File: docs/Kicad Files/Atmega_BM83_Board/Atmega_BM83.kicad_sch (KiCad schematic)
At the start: 34 parts, among them J1 18V, J10 ICE Header, J2 Out to Amp, J3 PWR SW, J4 Volume POT, J5 Pairing BTN, J6 PWR LED, J7 Pair LED, J8 Conn_01x12, J9 Conn_01x12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

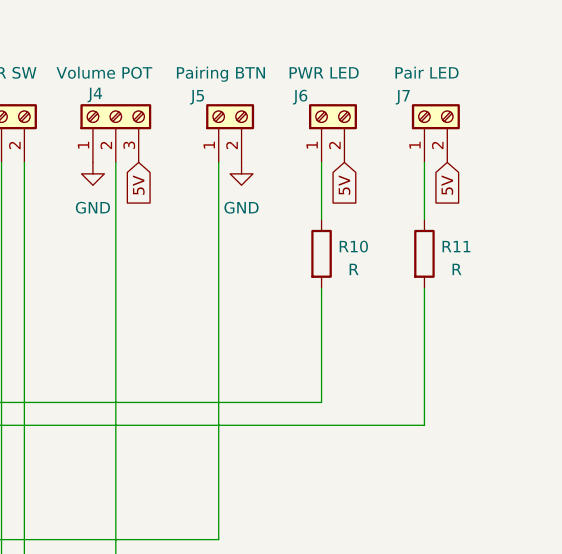
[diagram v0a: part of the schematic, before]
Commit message: all footprints assigned BM83/Atmega schematic
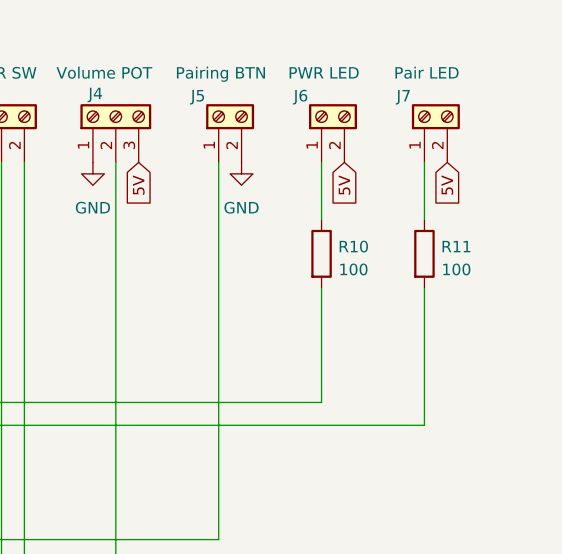
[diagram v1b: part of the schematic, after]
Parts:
- C1, C2, C3, C4: footprint (none) -> Capacitor_THT:CP_Radial_Tantal_D5.0mm_P5.00mm
- C6, C7: footprint (none) -> Capacitor_THT:C_Rect_L7.0mm_W2.5mm_P5.00mm
- J10: footprint Z_Custom_Footprints:ICE_Header -> Custom_Footprints:ICE_Header
- J4: footprint TerminalBlock_Phoenix:TerminalBlock_Phoenix_MKDS-1,5-3-5.08_1x03_P5.08mm_Horizontal -> TerminalBlock_Phoenix:TerminalBlock_Phoenix_MKDS-1,5-3_1x03_P5.00mm_Horizontal
- R10, R11: value R -> 100
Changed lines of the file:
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@@
 			)
 		)
-		(property "Footprint" ""
+		(property "Footprint" "Capacitor_THT:CP_Radial_Tantal_D5.0mm_P5.00mm"
 			(at 120.65 101.2952 0)
 			(effects
@@
 			)
 		)
-		(property "Footprint" ""
+		(property "Footprint" "Capacitor_THT:CP_Radial_Tantal_D5.0mm_P5.00mm"
 			(at 140.97 119.0752 0)
 			(effects
@@
 			)
 		)
-		(property "Footprint" ""
+		(property "Footprint" "Capacitor_THT:C_Rect_L7.0mm_W2.5mm_P5.00mm"
 			(at 163.5252 43.18 0)
 			(effects
@@
 			)
 		)
-		(property "Footprint" ""
+		(property "Footprint" "Capacitor_THT:CP_Radial_Tantal_D5.0mm_P5.00mm"
 			(at 69.85 101.9048 0)
 			(effects
@@
 			)
 		)
-		(property "Footprint" "Z_Custom_Footprints:ICE_Header"
+		(property "Footprint" "Custom_Footprints:ICE_Header"
 			(at 267.97 99.06 0)
 			(effects
@@
 			)
 		)
-		(property "Footprint" "TerminalBlock_Phoenix:TerminalBlock_Phoenix_MKDS-1,5-3-5.08_1x03_P5.08mm_Horizontal"
+		(property "Footprint" "TerminalBlock_Phoenix:TerminalBlock_Phoenix_MKDS-1,5-3_1x03_P5.00mm_Horizontal"
 			(at 238.76 25.4 0)
 			(effects
@@
 			)
 		)
-		(property "Value" "R"
+		(property "Value" "100"
 			(at 265.176 42.418 0)
 			(effects
@@
 			)
 		)
-		(property "Footprint" ""
+		(property "Footprint" "Capacitor_THT:C_Rect_L7.0mm_W2.5mm_P5.00mm"
 			(at 212.09 38.4048 0)
 			(effects
@@
 			)
 		)
-		(property "Footprint" ""
+		(property "Footprint" "Capacitor_THT:CP_Radial_Tantal_D5.0mm_P5.00mm"
 			(at 124.7648 45.72 0)
 			(effects
@@
 			)
 		)
-		(property "Value" "R"
+		(property "Value" "100"
 			(at 276.606 42.418 0)
 			(effects

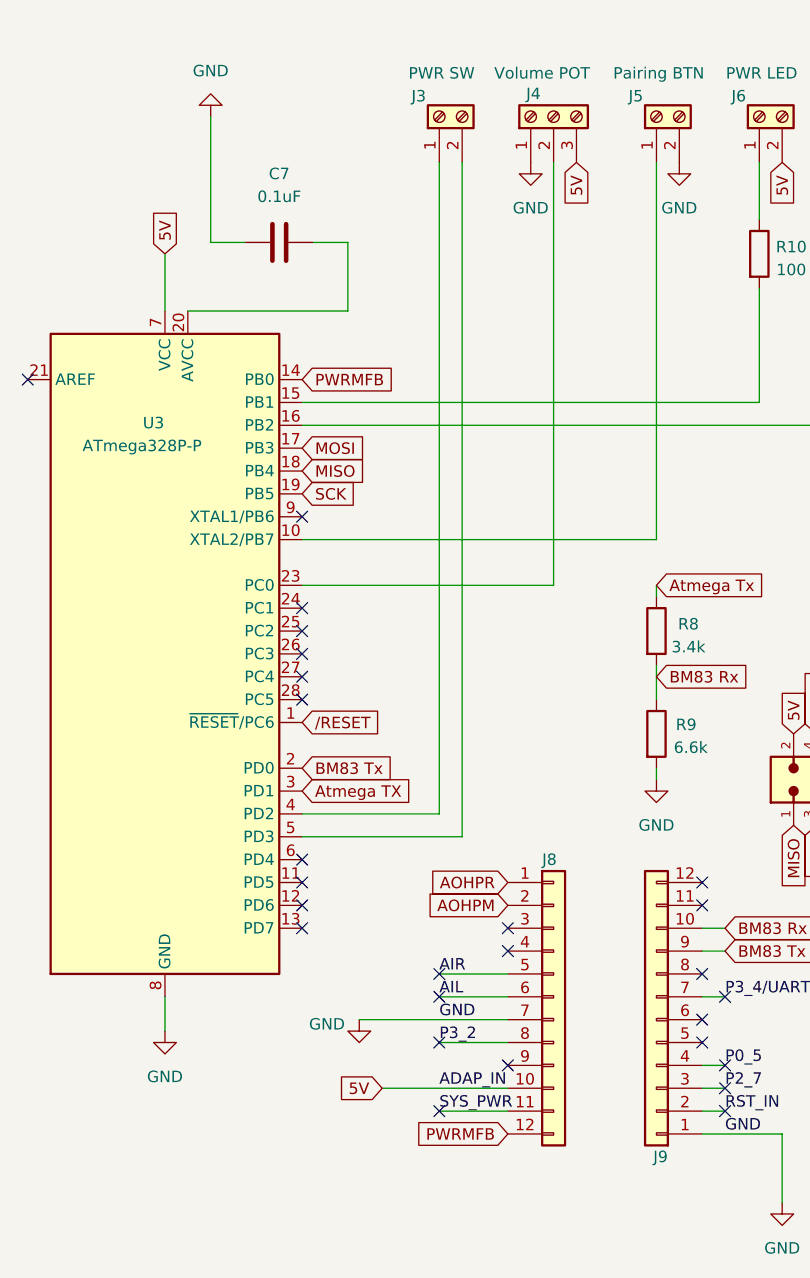
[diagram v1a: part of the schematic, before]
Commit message: changed volume switch and removed powerMFB
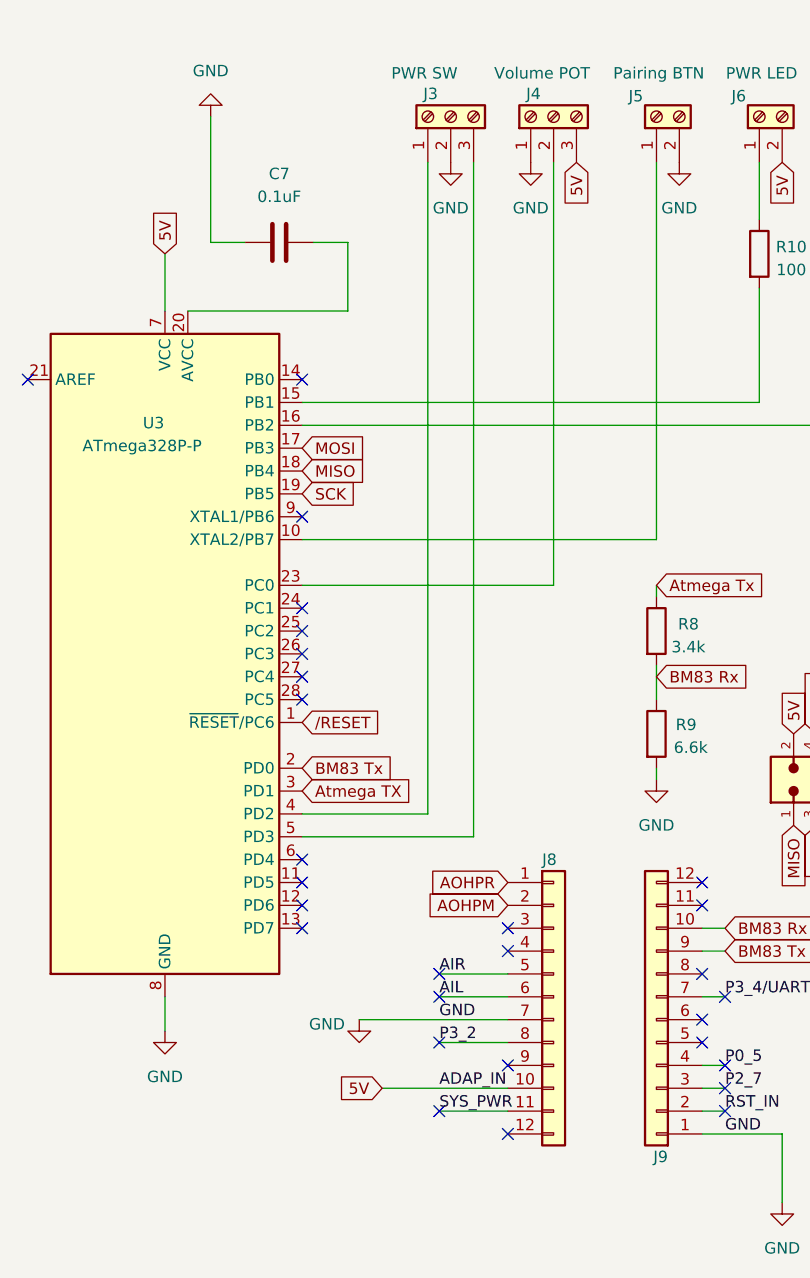
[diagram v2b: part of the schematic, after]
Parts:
- removed J3: PWR SW, TerminalBlock_Phoenix:TerminalBlock_Phoenix_MKDS-1,5-2_1x02_P5.00mm_Horizontal, symbol Connector:Screw_Terminal_01x02
- added J3: PWR SW, TerminalBlock_Phoenix:TerminalBlock_Phoenix_MKDS-1,5-3_1x03_P5.00mm_Horizontal, symbol Connector:Screw_Terminal_01x03
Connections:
- net GND: now also J3.2 (Pin_2)
- net at U3.4 (PD2): now also J3.1 (Pin_1)
- net at U3.5 (PD3): now also J3.3 (Pin_3)
- net PWRMFB: no longer names the net of J8.12 (Pin_12)
- net PWRMFB: no longer U3.14 (PB0)
- no-connect marks 27 -> 29
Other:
- title: (none) -> BM83/MC Module
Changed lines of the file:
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@@
 	(generator_version "8.0")
 	(paper "A4")
+	(title_block
+		(title "BM83/MC Module")
+	)
 	(junction
 		(at 137.16 118.11)
@@
 	)
 	(no_connect
+		(at 210.82 54.61)
+	)
+	(no_connect
+		(at 233.68 138.43)
+	)
+	(no_connect
 		(at 255.27 125.73)
 	)
@@
 	(wire
 		(pts
-			(xy 228.6 30.48) (xy 228.6 105.41)
+			(xy 229.87 30.48) (xy 229.87 105.41)
 		)
 		(stroke
@@
 	(wire
 		(pts
-			(xy 210.82 102.87) (xy 226.06 102.87)
+			(xy 210.82 102.87) (xy 224.79 102.87)
 		)
 		(stroke
@@
 	(wire
 		(pts
-			(xy 226.06 30.48) (xy 226.06 102.87)
+			(xy 224.79 30.48) (xy 224.79 102.87)
 		)
 		(stroke
@@
 	(wire
 		(pts
-			(xy 210.82 105.41) (xy 228.6 105.41)
+			(xy 210.82 105.41) (xy 229.87 105.41)
 		)
 		(stroke
@@
 		)
 	)
-	(global_label "PWRMFB"
-		(shape input)
-		(at 210.82 54.61 0)
-		(fields_autoplaced yes)
-		(effects
-			(font
-				(size 1.27 1.27)
-			)
-			(justify left)
-		)
-		(property "Intersheetrefs" "${INTERSHEET_REFS}"
-			(at 221.6066 54.61 0)
-			(effects
-				(font
-					(size 1.27 1.27)
-				)
-				(justify left)
-				(hide yes)
-			)
-		)
-	)
 	(global_label "18V"
 		(shape input)
@@
 		)
 	)
-	(global_label "PWRMFB"
-		(shape input)
-		(at 233.68 138.43 180)
-		(fields_autoplaced yes)
-		(effects
-			(font
-				(size 1.27 1.27)
-			)
-			(justify right)
-		)
-		(property "Intersheetrefs" "${INTERSHEET_REFS}"
-			(at 222.8934 138.43 0)
-			(effects
-				(font
-					(size 1.27 1.27)
-				)
-				(justify right)
-				(hide yes)
-			)
-		)
-	)
 	(global_label "{slash}RESET"
 		(shape input)
@@
 	)
 	(symbol
+		(lib_id "Connector:Screw_Terminal_01x03")
+		(at 227.33 25.4 90)
+		(unit 1)
+		(exclude_from_sim no)
+		(in_bom yes)
+		(on_board yes)
+		(dnp no)
+		(property "Reference" "J3"
+			(at 224.282 22.86 90)
+			(effects
+				(font
+					(size 1.27 1.27)
+				)
+				(justify right)
+			)
+		)
+		(property "Value" "PWR SW"
+			(at 220.726 20.574 90)
+			(effects
+				(font
+					(size 1.27 1.27)
+				)
+				(justify right)
+			)
+		)
+		(property "Footprint" "TerminalBlock_Phoenix:TerminalBlock_Phoenix_MKDS-1,5-3_1x03_P5.00mm_Horizontal"
+			(at 227.33 25.4 0)
+			(effects
+				(font
+					(size 1.27 1.27)
+				)
+				(hide yes)
+			)
+		)
+		(property "Datasheet" "~"
+			(at 227.33 25.4 0)
+			(effects
+				(font
+					(size 1.27 1.27)
+				)
+				(hide yes)
+			)
+		)
+		(property "Description" "Generic screw terminal, single row, 01x03, script generated (kicad-library-utils/schlib/autogen/connector/)"
+			(at 227.33 25.4 0)
+			(effects
+				(font
+					(size 1.27 1.27)
+				)
+				(hide yes)
+			)
+		)
+		(pin "1"
+		)
+		(pin "2"
+		)
+		(pin "3"
+		)
+		(instances
+			(project "Atmega_BM83"
+				(path "/b3cfe92d-97c3-48fc-9671-6e68a58d7c48"
+					(reference "J3")
+					(unit 1)
+				)
+			)
+		)
+	)
+	(symbol
 		(lib_id "Mechanical:MountingHole_Pad")
 		(at 71.12 46.99 270)
@@
 	)
 	(symbol
-		(lib_id "Connector:Screw_Terminal_01x02")
-		(at 226.06 25.4 90)
-		(unit 1)
-		(exclude_from_sim no)
-		(in_bom yes)
-		(on_board yes)
-		(dnp no)
-		(property "Reference" "J3"
-			(at 223.774 23.114 90)
-			(effects
-				(font
-					(size 1.27 1.27)
-				)
-			)
-		)
-		(property "Value" "PWR SW"
-			(at 226.314 20.574 90)
-			(effects
-				(font
-					(size 1.27 1.27)
-				)
-			)
-		)
-		(property "Footprint" "TerminalBlock_Phoenix:TerminalBlock_Phoenix_MKDS-1,5-2_1x02_P5.00mm_Horizontal"
-			(at 226.06 25.4 0)
-			(effects
-				(font
-					(size 1.27 1.27)
-				)
-				(hide yes)
-			)
-		)
-		(property "Datasheet" "~"
-			(at 226.06 25.4 0)
-			(effects
-				(font
-					(size 1.27 1.27)
-				)
-				(hide yes)
-			)
-		)
-		(property "Description" "Generic screw terminal, single row, 01x02, script generated (kicad-library-utils/schlib/autogen/connector/)"
-			(at 226.06 25.4 0)
-			(effects
-				(font
-					(size 1.27 1.27)
-				)
-				(hide yes)
-			)
-		)
-		(pin "1"
-		)
-		(pin "2"
-		)
-		(instances
-			(project "Atmega_BM83"
-				(path "/b3cfe92d-97c3-48fc-9671-6e68a58d7c48"
-					(reference "J3")
-					(unit 1)
-				)
-			)
-		)
-	)
-	(symbol
 		(lib_id "power:GND")
 		(at 217.17 125.73 0)
@@
 					(unit 1)
 				)
+			)
+		)
+	)
+	(symbol
+		(lib_id "power:GND")
+		(at 227.33 30.48 0)
+		(unit 1)
+		(exclude_from_sim no)
+		(in_bom yes)
+		(on_board yes)
+		(dnp no)
+		(fields_autoplaced yes)
+		(property "Reference" "#PWR014"
+			(at 227.33 36.83 0)
+			(effects
+				(font
+					(size 1.27 1.27)
+				)
+				(hide yes)
+			)
+		)
+		(property "Value" "GND"
+			(at 227.33 35.56 0)
+			(effects
+				(font
+					(size 1.27 1.27)
+				)
+			)
+		)
+		(property "Footprint" ""
+			(at 227.33 30.48 0)
+			(effects
+				(font
+					(size 1.27 1.27)
+				)
+				(hide yes)
+			)
+		)
+		(property "Datasheet" ""
+			(at 227.33 30.48 0)
+			(effects
+				(font
+					(size 1.27 1.27)
+				)
+				(hide yes)
+			)
+		)
+		(property "Description" "Power symbol creates a global label with name \"GND\" , ground"
+			(at 227.33 30.48 0)
+			(effects
+				(font
+					(size 1.27 1.27)
+				)
+				(hide yes)
+			)
+		)
+		(pin "1"
+		)
+		(instances
+			(project "Atmega_BM83"
+				(path "/b3cfe92d-97c3-48fc-9671-6e68a58d7c48"
+					(reference "#PWR014")
+					(unit 1)
+				)

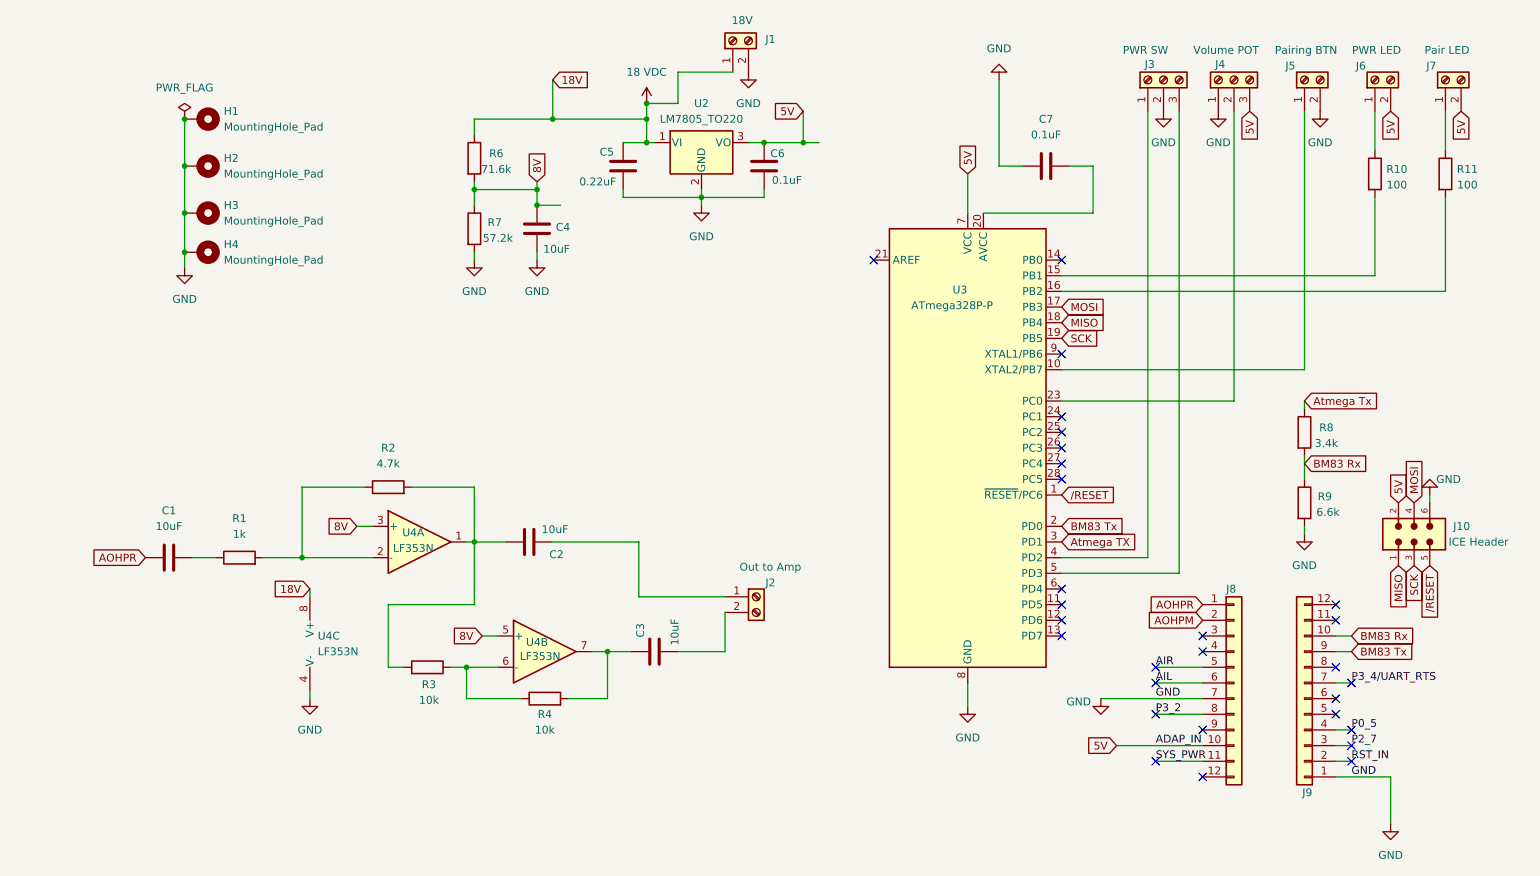
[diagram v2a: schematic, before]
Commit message: final changes to BM83/Atmega schematic
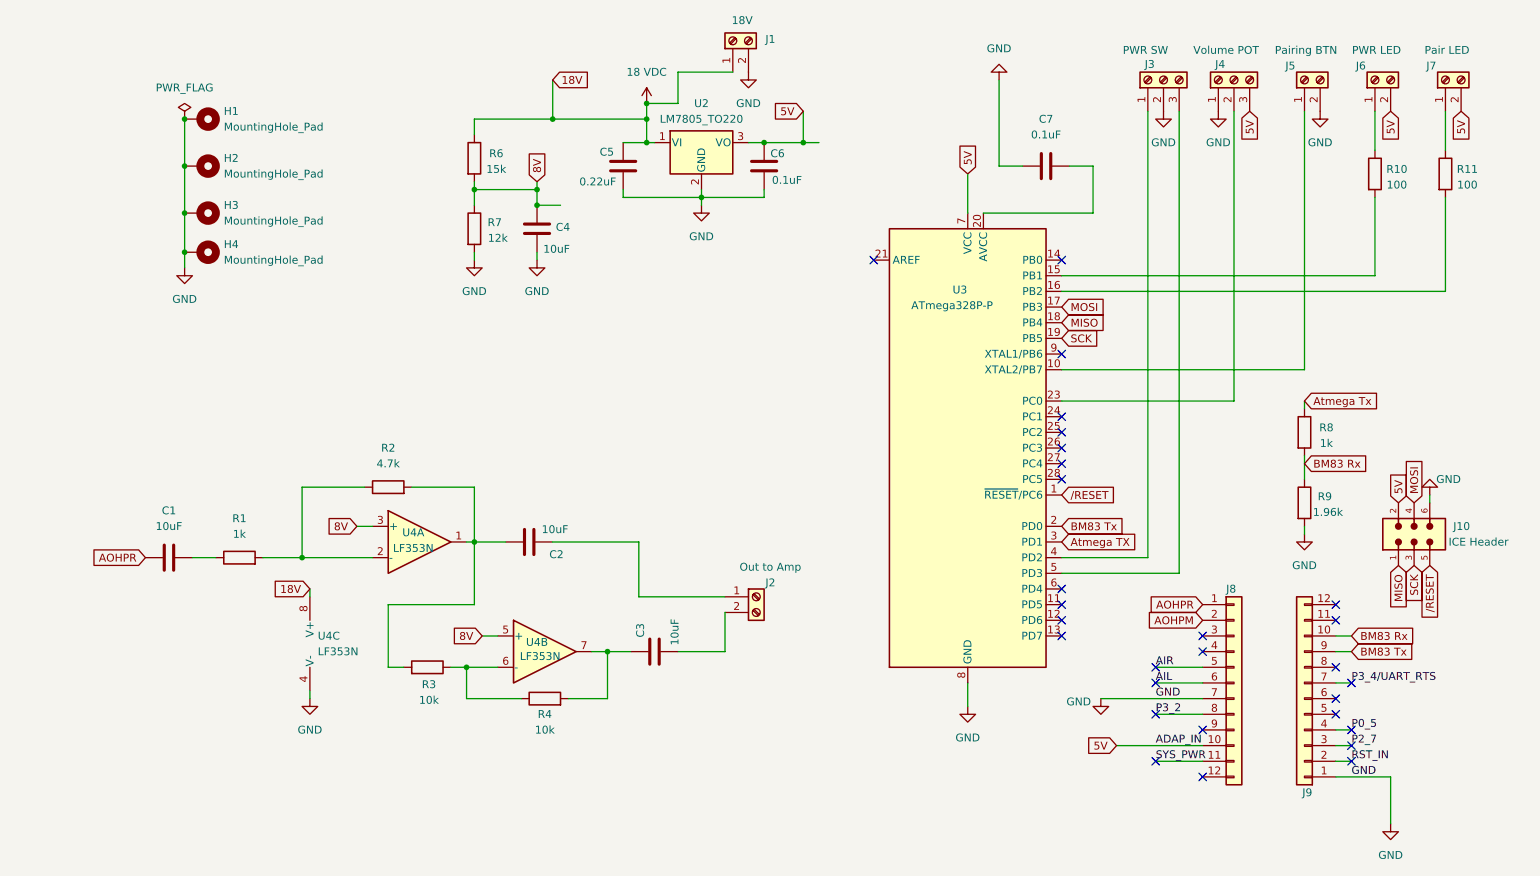
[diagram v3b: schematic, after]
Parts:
- R6: value 71.6k -> 15k
- R7: value 57.2k -> 12k
- R8: value 3.4k -> 1k
- R9: value 6.6k -> 1.96k
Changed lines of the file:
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@@
 			)
 		)
-		(property "Value" "71.6k"
+		(property "Value" "15k"
 			(at 119.126 39.878 0)
 			(effects
@@
 			)
 		)
-		(property "Value" "3.4k"
+		(property "Value" "1k"
 			(at 253.746 84.328 0)
 			(effects
@@
 			)
 		)
-		(property "Value" "6.6k"
+		(property "Value" "1.96k"
 			(at 254 95.504 0)
 			(effects
@@
 			)
 		)
-		(property "Value" "57.2k"
+		(property "Value" "12k"
 			(at 119.38 51.054 0)
 			(effects
